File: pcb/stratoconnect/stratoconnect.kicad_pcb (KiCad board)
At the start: 2 copper layers, 61.8 x 40 mm, 16 parts, among them J1 Conn_Coaxial, J2 Conn_02x03_Odd_Even, J3 Conn_01x05_Male, J4 Conn_01x02_Male, J5 Conn_01x03_Male, SW1 SW_SPST, U1 RF4463f30, U2 ATmega328PB-A, Y1 CSTNE16M0V530000R0

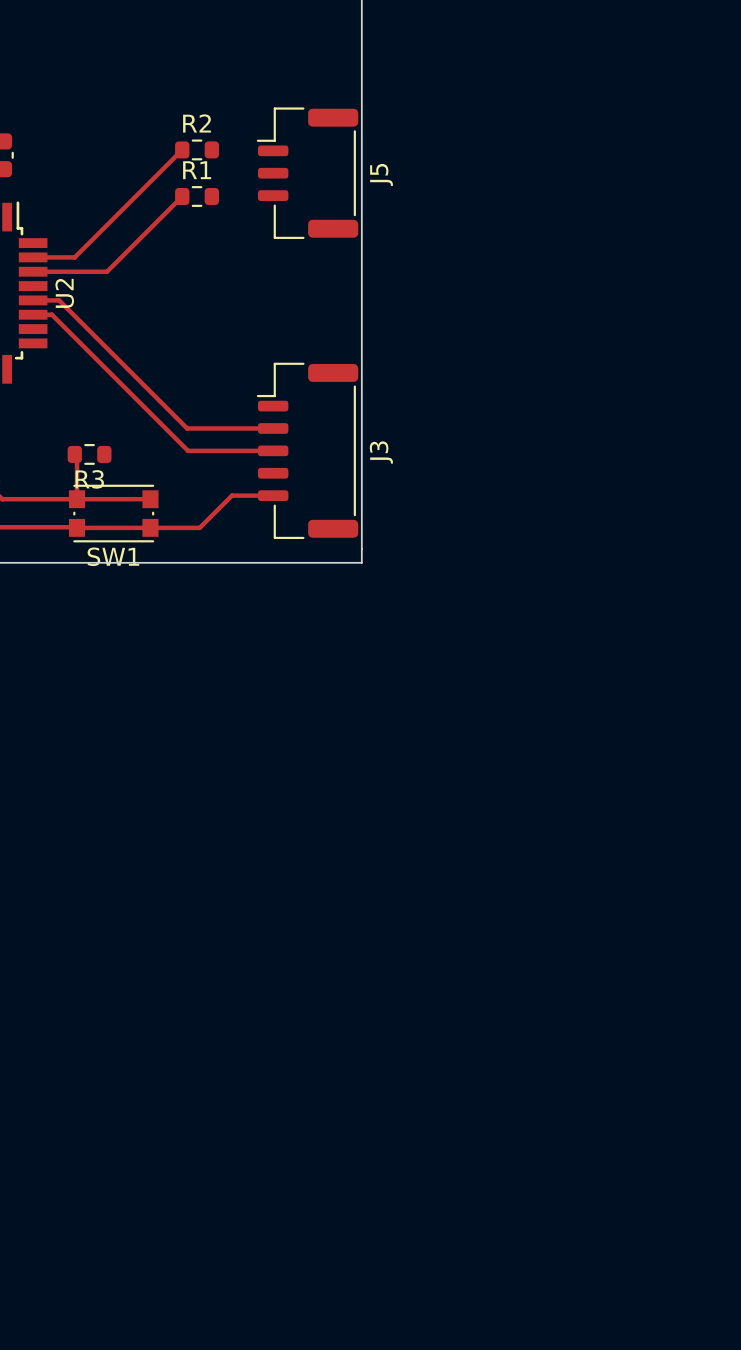
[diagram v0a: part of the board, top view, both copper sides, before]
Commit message: add 6060 Inductor foodprint
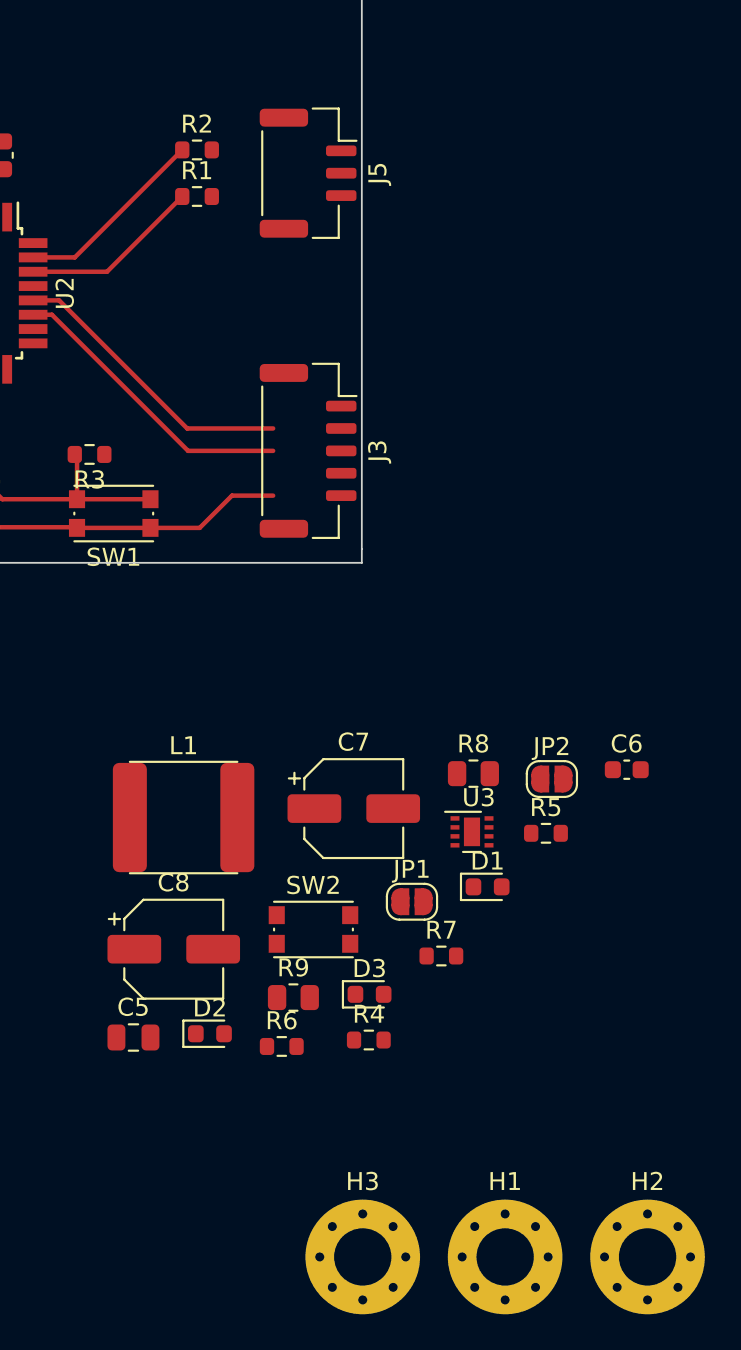
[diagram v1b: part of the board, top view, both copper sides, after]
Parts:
- added C5: 10uF, Capacitor_SMD:C_0805_2012Metric, F.Cu at (188.2, 116.8)
- added C6: 100nF, Capacitor_SMD:C_0603_1608Metric, F.Cu at (215.8, 101.8)
- added C7: 47uF, Capacitor_SMD:CP_Elec_5x5.3, F.Cu at (200.6, 104.0)
- added C8: 50uF, Capacitor_SMD:CP_Elec_5x5.3, F.Cu at (190.5, 111.8)
- added D1: LED, LED_SMD:LED_0603_1608Metric, F.Cu at (208.0, 108.3)
- added D2: LED, LED_SMD:LED_0603_1608Metric, F.Cu at (192.5, 116.5)
- added D3: LED, LED_SMD:LED_0603_1608Metric, F.Cu at (201.4, 114.3)
- added H1: MountingHole_Pad, MountingHole:MountingHole_3.2mm_M3_Pad_Via, F.Cu at (209.0, 129.0)
- added H2: MountingHole_Pad, MountingHole:MountingHole_3.2mm_M3_Pad_Via, F.Cu at (216.9, 129.0)
- added H3: MountingHole_Pad, MountingHole:MountingHole_3.2mm_M3_Pad_Via, F.Cu at (201.1, 129.0)
- added JP1: SolderJumper_2_Open, Jumper:SolderJumper-2_P1.3mm_Open_RoundedPad1.0x1.5mm, F.Cu at (203.8, 109.2)
- added JP2: SolderJumper_2_Open, Jumper:SolderJumper-2_P1.3mm_Open_RoundedPad1.0x1.5mm, F.Cu at (211.6, 102.3)
- added L1: 1u, Inductor_SMD:L_2440_6060Metric, F.Cu at (191.1, 104.5)
- added R4: 10k, Resistor_SMD:R_0603_1608Metric, F.Cu at (201.4, 116.9)
- added R5: 220, Resistor_SMD:R_0603_1608Metric, F.Cu at (211.3, 105.3)
- added R6: 220, Resistor_SMD:R_0603_1608Metric, F.Cu at (196.5, 117.2)
- added R7: 220, Resistor_SMD:R_0603_1608Metric, F.Cu at (205.4, 112.2)
- added R8: 732k, Resistor_SMD:R_0805_2012Metric, F.Cu at (207.2, 102.0)
- added R9: 100k, Resistor_SMD:R_0805_2012Metric, F.Cu at (197.2, 114.5)
- added SW2: SW_SPST, Button_Switch_SMD:SW_Push_1P1T_NO_CK_KMR2, F.Cu at (198.3, 110.7)
- added U3: TPS61022RWU, Package_SON:WSON-8-1EP_2x2mm_P0.5mm_EP0.9x1.6mm, F.Cu at (207.2, 105.3)
- J3: footprint Connector_JST:JST_GH_BM05B-GHS-TBT_1x05-1MP_P1.25mm_Vertical -> Connector_JST:JST_GH_SM05B-GHS-TB_1x05-1MP_P1.25mm_Horizontal
- J5: footprint Connector_JST:JST_GH_BM03B-GHS-TBT_1x03-1MP_P1.25mm_Vertical -> Connector_JST:JST_GH_SM03B-GHS-TB_1x03-1MP_P1.25mm_Horizontal
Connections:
- J2 pad 1: /MISO -> /SPI_MISO
- J2 pad 3: /SCK -> /SPI_SCK
- J2 pad 4: /MOSI -> /SPI_MOSI
- J3 pad 4: +3V3 -> +5V
- R1 pad 2: /TX -> /UART_TX
- R2 pad 2: /RX -> /UART_RX
- U1 pad 10: /~{CS} -> /~{SPI_CS_SW}
- U1 pad 6: /MISO -> /SPI_MISO
- U1 pad 7: /MOSI -> /SPI_MOSI
- U1 pad 8: /SCK -> /SPI_SCK
- U2 pad 1: unconnected-(U2-Pad1) -> /LED_TX
- U2 pad 13: unconnected-(U2-Pad13) -> /~{SPI_CS}
- U2 pad 14: /~{CS} -> unconnected-(U2-Pad14)
- U2 pad 15: /MOSI -> unconnected-(U2-Pad15)
- U2 pad 16: /MISO -> unconnected-(U2-Pad16)
- U2 pad 17: /SCK -> unconnected-(U2-Pad17)
- U2 pad 19: unconnected-(U2-Pad19) -> /SPI_SCK
- U2 pad 2: unconnected-(U2-Pad2) -> /LED_RX
- U2 pad 3: unconnected-(U2-Pad3) -> /SPI_MOSI
- U2 pad 6: unconnected-(U2-Pad6) -> /SPI_MISO

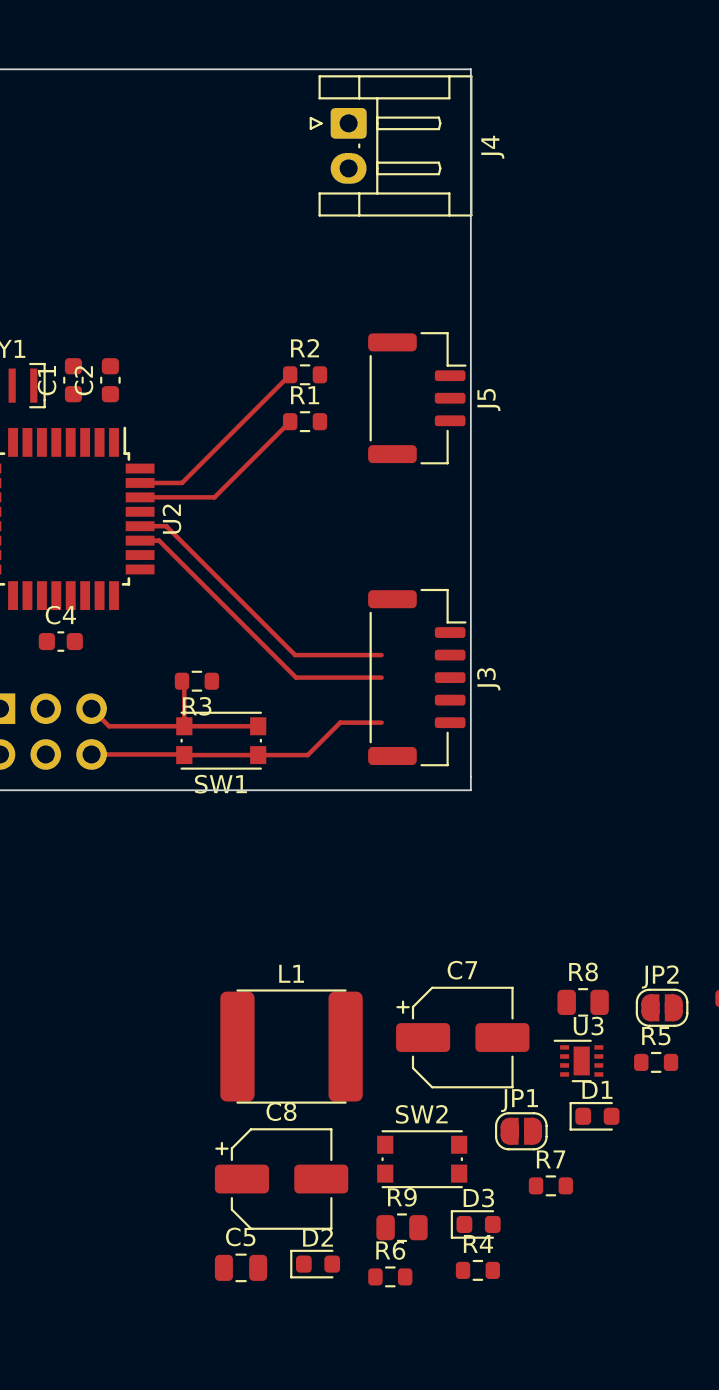
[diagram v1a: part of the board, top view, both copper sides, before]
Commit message: build out the VQFN7-7 footbring for the boost converter
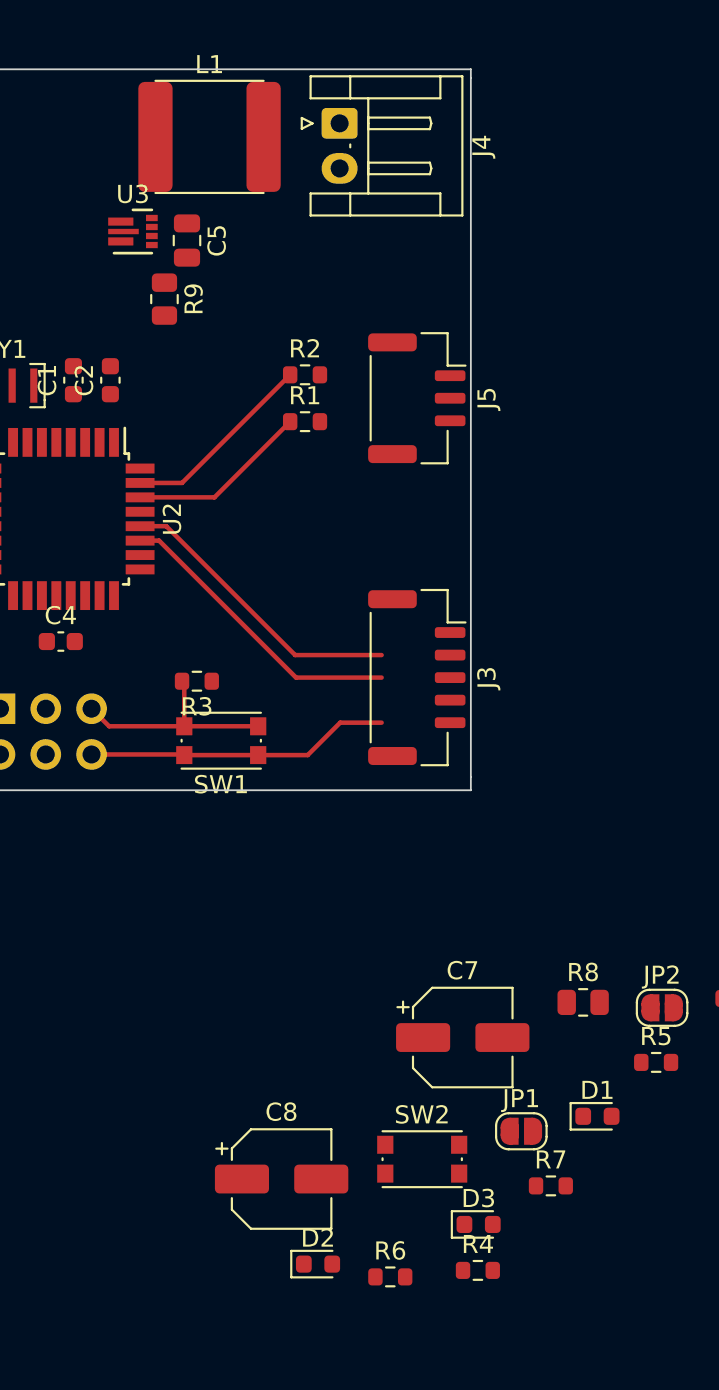
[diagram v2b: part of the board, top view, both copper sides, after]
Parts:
- U3: footprint Package_SON:WSON-8-1EP_2x2mm_P0.5mm_EP0.9x1.6mm -> Package_DFN_QFN:VDFN-7_2.1x2.1mm
- moved C5 57.1 mm to (185.2, 59.8), turned to -90 degrees
- moved R9 53.2 mm to (184.0, 63.0), turned to -90 degrees
- moved U3 52.3 mm to (182.2, 59.2)
- moved L1 50.7 mm to (186.5, 54.0)
- moved J4 0.50 mm to (193.7, 53.2)

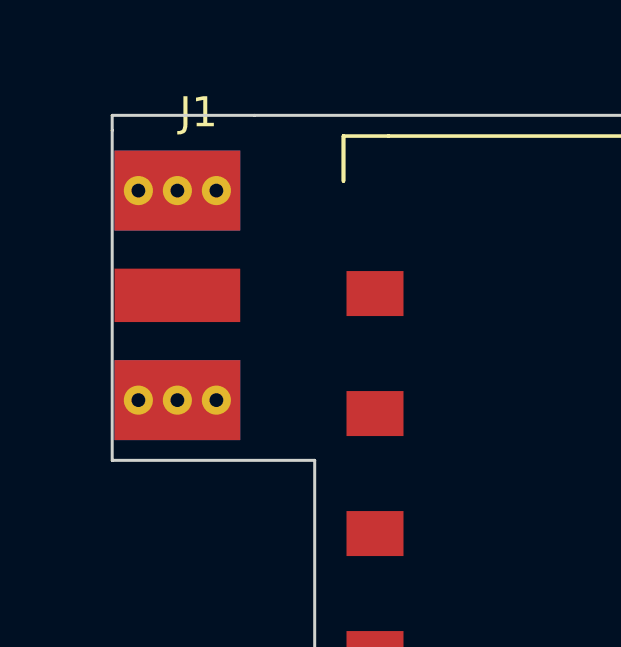
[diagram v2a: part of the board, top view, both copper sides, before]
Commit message: update schematic to add mroe room for the smps
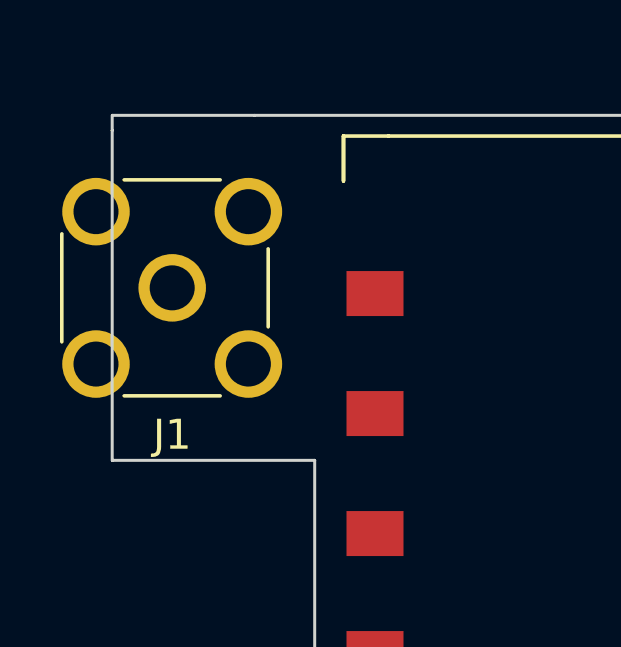
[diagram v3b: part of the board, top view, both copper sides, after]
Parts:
- J1: footprint Connector_Coaxial:SMA_Molex_73251-2120_EdgeMount_Horizontal -> Connector_Coaxial:SMA_Molex_73251-2200_Horizontal
- moved J1 0.30 mm to (141.2, 56.0), turned to 90 degrees
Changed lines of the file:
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@@
     )
   )
-  (footprint "Connector_Coaxial:SMA_Molex_73251-2120_EdgeMount_Horizontal" (layer "F.Cu")
-    (at 141.4225 56.25 180)
-    (descr "Molex SMA RF Connector, Edge Mount, (http://www.molex.com/pdm_docs/sd/732512120_sd.pdf)")
-    (tags "sma edge")
+  (footprint "Connector_Coaxial:SMA_Molex_73251-2200_Horizontal" (layer "F.Cu")
+    (at 141.25 56 90)
+    (descr "https://www.molex.com/webdocs/datasheets/pdf/en-us/0732512200_RF_COAX_CONNECTORS.pdf")
+    (tags "SMA THT Female Jack Horizontal")
     (property "Sheetfile" "stratoconnect.kicad_sch")
     (property "Sheetname" "")
-    (attr smd)
-    (fp_text reference "J1" (at -0.705 6.1) (layer "F.SilkS")
+    (attr through_hole)
+    (fp_text reference "J1" (at -4.9 0) (layer "F.SilkS")
       (effects (font (size 1 1) (thickness 0.15)))
     )
-    (fp_text value "Conn_Coaxial" (at -0.1 -6.2) (layer "F.Fab")
+    (fp_text value "Conn_Coaxial" (at 0 5 90) (layer "F.Fab")
       (effects (font (size 1 1) (thickness 0.15)))
     )
-    (fp_text user "PCB Edge" (at 2.155 0 90) (layer "Dwgs.User")
-      (effects (font (size 0.5 0.5) (thickness 0.08)))
-    )
-    (fp_text user "${REFERENCE}" (at 9.095 0) (layer "F.Fab")
+    (fp_text user "${REFERENCE}" (at 0 0 90) (layer "F.Fab")
       (effects (font (size 1 1) (thickness 0.15)))
     )
-    (fp_line (start -2.7 -5.33) (end 15.045 -5.33) (layer "B.CrtYd") (width 0.05))
-    (fp_line (start -2.7 -5.33) (end -2.7 5.33) (layer "B.CrtYd") (width 0.05))
-    (fp_line (start 15.045 5.33) (end -2.7 5.33) (layer "B.CrtYd") (width 0.05))
-    (fp_line (start 15.045 -5.33) (end 15.045 5.33) (layer "B.CrtYd") (width 0.05))
-    (fp_line (start -2.7 -5.33) (end 15.045 -5.33) (layer "F.CrtYd") (width 0.05))
-    (fp_line (start -2.7 -5.33) (end -2.7 5.33) (layer "F.CrtYd") (width 0.05))
-    (fp_line (start 15.045 5.33) (end -2.7 5.33) (layer "F.CrtYd") (width 0.05))
-    (fp_line (start 15.045 -5.33) (end 15.045 5.33) (layer "F.CrtYd") (width 0.05))
-    (fp_line (start -1.715 3.175) (end -1.715 2.155) (layer "F.Fab") (width 0.1))
-    (fp_line (start 2.9 0) (end 2.095 0.635) (layer "F.Fab") (width 0.1))
-    (fp_line (start 2.095 -0.635) (end -1.715 -0.635) (layer "F.Fab") (width 0.1))
-    (fp_line (start 3.115 3.175) (end -1.715 3.175) (layer "F.Fab") (width 0.1))
-    (fp_line (start -1.715 -3.175) (end 3.115 -3.175) (layer "F.Fab") (width 0.1))
-    (fp_line (start 2.095 2.155) (end -1.715 2.155) (layer "F.Fab") (width 0.1))
-    (fp_line (start 2.095 -2.155) (end -1.715 -2.155) (layer "F.Fab") (width 0.1))
-    (fp_line (start -1.715 -3.175) (end -1.715 -2.155) (layer "F.Fab") (width 0.1))
-    (fp_line (start 3.115 -3.175) (end 3.115 3.175) (layer "F.Fab") (width 0.1))
-    (fp_line (start 2.095 -0.635) (end 2.9 0) (layer "F.Fab") (width 0.1))
-    (fp_line (start -1.715 -0.635) (end -1.715 0.635) (layer "F.Fab") (width 0.1))
-    (fp_line (start 2.095 -2.155) (end 2.095 2.155) (layer "F.Fab") (width 0.1))
-    (fp_line (start 14.545 -2.64) (end 3.115 -2.64) (layer "F.Fab") (width 0.1))
-    (fp_line (start 2.095 0.635) (end -1.715 0.635) (layer "F.Fab") (width 0.1))
-    (fp_line (start 14.545 -2.64) (end 14.545 2.64) (layer "F.Fab") (width 0.1))
-    (fp_line (start 14.545 2.64) (end 3.115 2.64) (layer "F.Fab") (width 0.1))
-    (pad "1" smd rect (at 0 0 180) (size 4.19 1.78) (layers "F.Cu" "F.Paste" "F.Mask")
+    (fp_line (start -1.8 -3.68) (end 1.8 -3.68) (layer "F.SilkS") (width 0.12))
+    (fp_line (start -3.6 -1.6) (end -3.6 1.6) (layer "F.SilkS") (width 0.12))
+    (fp_line (start 3.6 -1.6) (end 3.6 1.6) (layer "F.SilkS") (width 0.12))
+    (fp_line (start -1.3 3.2) (end 1.3 3.2) (layer "F.SilkS") (width 0.12))
+    (fp_line (start 4.4 4.16) (end -4.4 4.16) (layer "F.CrtYd") (width 0.05))
+    (fp_line (start -4.4 -17) (end 4.4 -17) (layer "F.CrtYd") (width 0.05))
+    (fp_line (start -4.4 -17) (end -4.4 4.16) (layer "F.CrtYd") (width 0.05))
+    (fp_line (start 4.4 4.16) (end 4.4 -17) (layer "F.CrtYd") (width 0.05))
+    (fp_line (start 3.9 -3.95) (end 3.9 -5.07) (layer "F.Fab") (width 0.1))
+    (fp_line (start -3 -16.5) (end -3 -5.07) (layer "F.Fab") (width 0.1))
+    (fp_line (start -3 -16.5) (end 3 -16.5) (layer "F.Fab") (width 0.1))
+    (fp_line (start -3 -12) (end 3 -12.7) (layer "F.Fab") (width 0.1))
+    (fp_line (start -3 -8) (end 3 -8.7) (layer "F.Fab") (width 0.1))
+    (fp_line (start -3 -13) (end 3 -13.7) (layer "F.Fab") (width 0.1))
+    (fp_line (start 3 -16.5) (end 3 -5.07) (layer "F.Fab") (width 0.1))
+    (fp_line (start -3 -6) (end 3 -6.7) (layer "F.Fab") (width 0.1))
+    (fp_line (start 3.5 -3.95) (end 3.5 3.05) (layer "F.Fab") (width 0.1))
+    (fp_line (start -3 -11) (end 3 -11.7) (layer "F.Fab") (width 0.1))
+    (fp_line (start -3.5 -3.95) (end -3.5 3.05) (layer "F.Fab") (width 0.1))
+    (fp_line (start -3.9 -3.95) (end 3.9 -3.95) (layer "F.Fab") (width 0.1))
+    (fp_line (start -3 -9) (end 3 -9.7) (layer "F.Fab") (width 0.1))
+    (fp_line (start -3.5 3.05) (end 3.5 3.05) (layer "F.Fab") (width 0.1))
+    (fp_line (start 3.9 -5.07) (end -3.9 -5.07) (layer "F.Fab") (width 0.1))
+    (fp_line (start -3.9 -5.07) (end -3.9 -3.95) (layer "F.Fab") (width 0.1))
+    (fp_line (start -3 -14) (end 3 -14.7) (layer "F.Fab") (width 0.1))
+    (fp_line (start -3 -7) (end 3 -7.7) (layer "F.Fab") (width 0.1))
+    (fp_line (start -3.5 -3.95) (end 3.5 -3.95) (layer "F.Fab") (width 0.1))
+    (fp_line (start -3 -10) (end 3 -10.7) (layer "F.Fab") (width 0.1))
+    (pad "1" thru_hole circle (at 0 0 90) (size 2.25 2.25) (drill 1.5) (layers *.Cu *.Mask)
       (net 11 "Net-(J1-Pad1)") (pinfunction "In") (pintype "passive"))
-    (pad "2" thru_hole circle (at 1.3 -3.4925 180) (size 0.97 0.97) (drill 0.46) (layers *.Cu)
+    (pad "2" thru_hole circle (at -2.54 2.54 90) (size 2.25 2.25) (drill 1.5) (layers *.Cu *.Mask)
       (net 12 "Net-(J1-Pad2)") (pinfunction "Ext") (pintype "passive"))
-    (pad "2" smd rect (at 0 3.4925 180) (size 4.19 2.665) (layers "F.Cu" "F.Paste" "F.Mask")
+    (pad "2" thru_hole circle (at 2.54 2.54 180) (size 2.25 2.25) (drill 1.5) (layers *.Cu *.Mask)
       (net 12 "Net-(J1-Pad2)") (pinfunction "Ext") (pintype "passive"))
-    (pad "2" thru_hole circle (at -1.3 3.4925 180) (size 0.97 0.97) (drill 0.46) (layers *.Cu)
+    (pad "2" thru_hole circle (at -2.54 -2.54 90) (size 2.25 2.25) (drill 1.5) (layers *.Cu *.Mask)
       (net 12 "Net-(J1-Pad2)") (pinfunction "Ext") (pintype "passive"))
-    (pad "2" smd rect (at 0 -3.4925 180) (size 4.19 2.665) (layers "B.Cu" "B.Paste" "B.Mask")
+    (pad "2" thru_hole circle (at 2.54 -2.54 90) (size 2.25 2.25) (drill 1.5) (layers *.Cu *.Mask)
       (net 12 "Net-(J1-Pad2)") (pinfunction "Ext") (pintype "passive"))
-    (pad "2" thru_hole circle (at 0 -3.4925 180) (size 0.97 0.97) (drill 0.46) (layers *.Cu)
-      (net 12 "Net-(J1-Pad2)") (pinfunction "Ext") (pintype "passive"))
-    (pad "2" thru_hole circle (at 1.3 3.4925 180) (size 0.97 0.97) (drill 0.46) (layers *.Cu)
-      (net 12 "Net-(J1-Pad2)") (pinfunction "Ext") (pintype "passive"))
-    (pad "2" smd rect (at 0 3.4925 180) (size 4.19 2.665) (layers "B.Cu" "B.Paste" "B.Mask")
-      (net 12 "Net-(J1-Pad2)") (pinfunction "Ext") (pintype "passive"))
-    (pad "2" smd rect (at 0 -3.4925 180) (size 4.19 2.665) (layers "F.Cu" "F.Paste" "F.Mask")
-      (net 12 "Net-(J1-Pad2)") (pinfunction "Ext") (pintype "passive"))
-    (pad "2" thru_hole circle (at -1.3 -3.4925 180) (size 0.97 0.97) (drill 0.46) (layers *.Cu)
-      (net 12 "Net-(J1-Pad2)") (pinfunction "Ext") (pintype "passive"))
-    (pad "2" thru_hole circle (at 0 3.4925 180) (size 0.97 0.97) (drill 0.46) (layers *.Cu)
-      (net 12 "Net-(J1-Pad2)") (pinfunction "Ext") (pintype "passive"))
-    (model "/Users/kevinlutzer/Projects/Kevin-Lutzer-Kicad-Lbr/Kevin_Lutzer_Lbr.3shapes/SMA_female_edge_6.5x6.5.step"
-      (offset (xyz -0.4 0 0))
+    (model "${KICAD6_3DMODEL_DIR}/Connector_Coaxial.3dshapes/SMA_Molex_73251-2200_Horizontal.wrl"
+      (offset (xyz 0 0 0))
       (scale (xyz 1 1 1))
-      (rotate (xyz 0 1 -90))
+      (rotate (xyz 0 0 0))
     )
   )
